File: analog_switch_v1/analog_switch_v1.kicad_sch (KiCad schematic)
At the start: 46 parts, among them J1 Conn_02x05_Odd_Even, J2 Audio In, J3 Audio Out, J4 Gate In, Q1 BC547, Q2 BC547, Q3 BC547, SW1 SW_GATE, U1 L78L05_SOT89, U2 TL072, U3 DG418LDJ

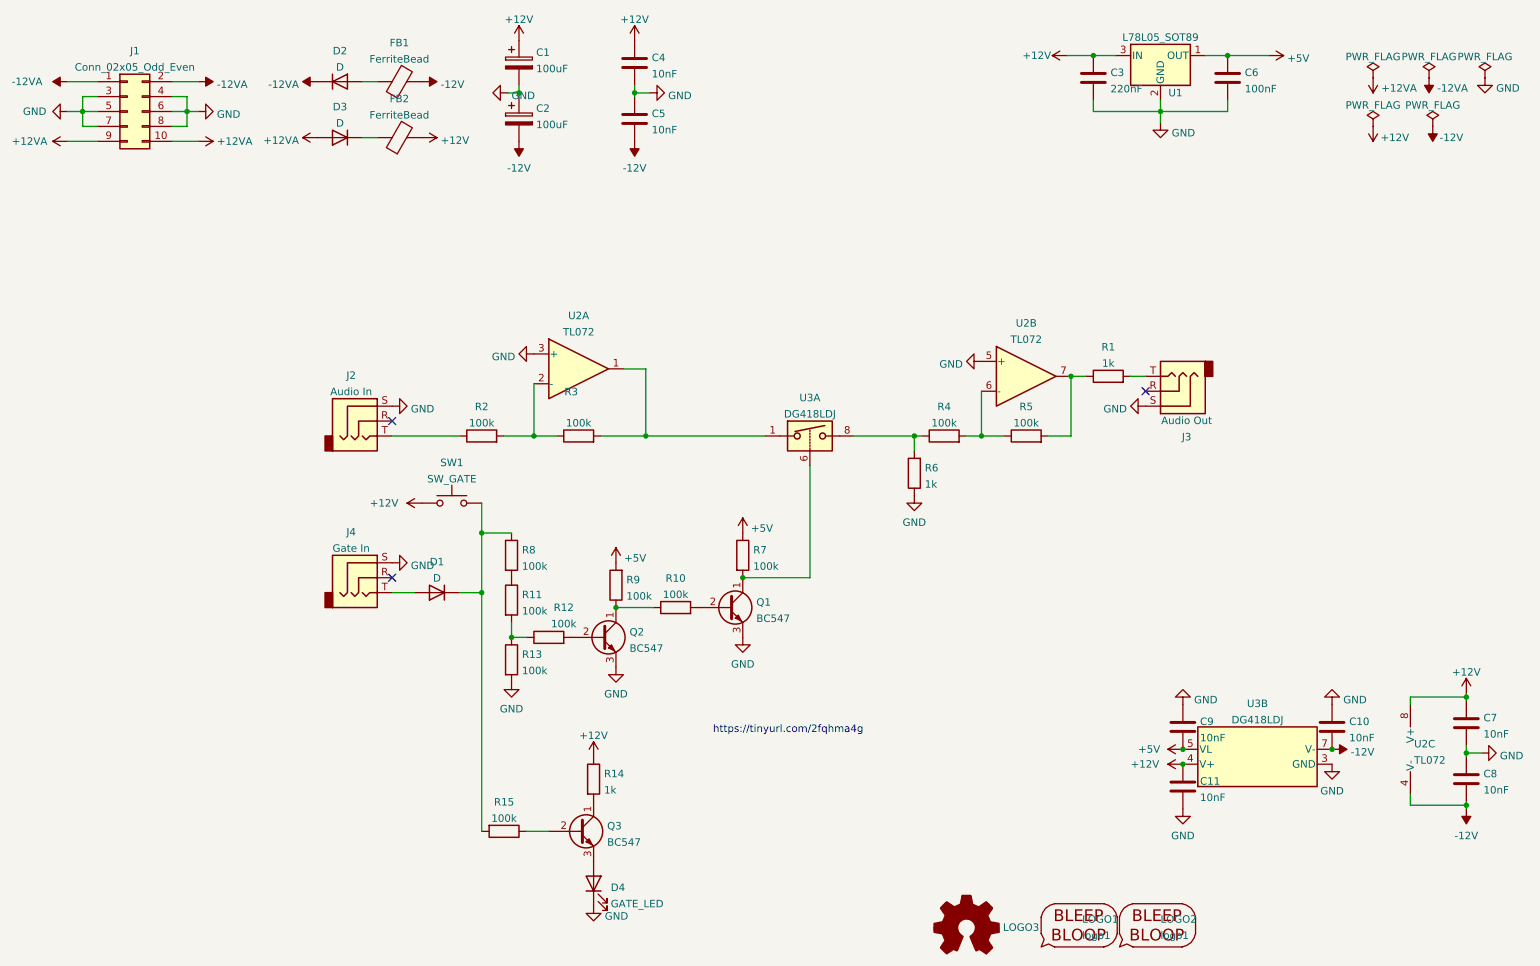
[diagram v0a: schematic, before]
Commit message: Geographic re-annotate and silkscreen cleanup
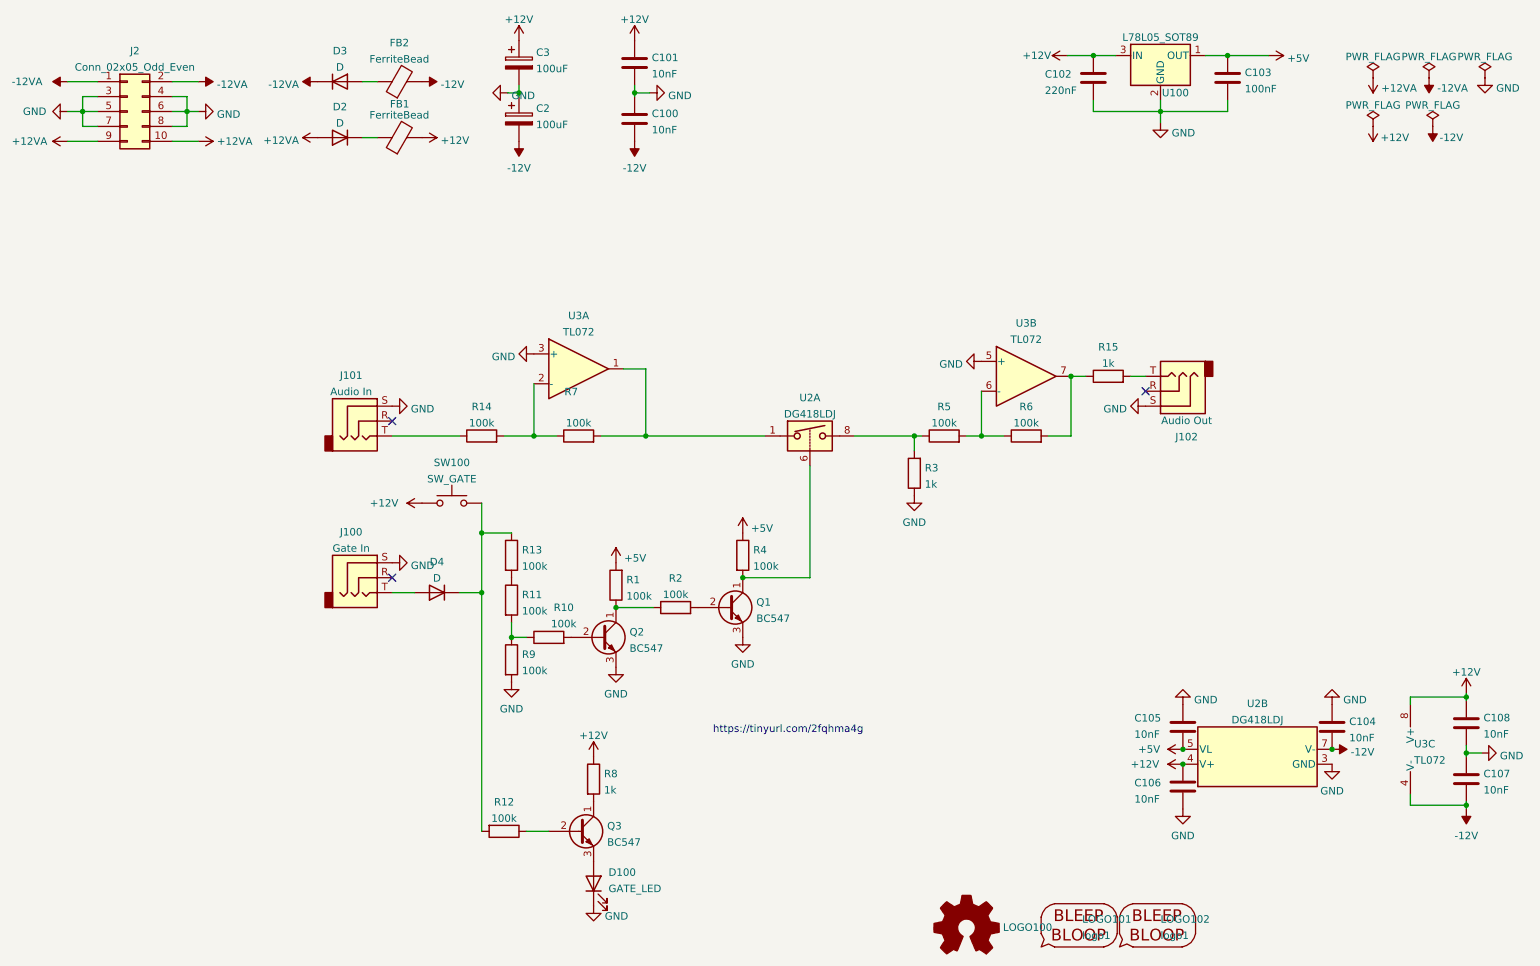
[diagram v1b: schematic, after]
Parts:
- renumbered C5 to C100, C4 to C101, C3 to C102, C6 to C103, C10 to C104, C9 to C105, C11 to C106, C8 to C107, C7 to C108, C1 to C3, D4 to D100, D3 to D2, D2 to D3, D1 to D4, FB2 to FB1, FB1 to FB2, J4 to J100, J2 to J101, J3 to J102, J1 to J2, LOGO3 to LOGO100, LOGO1 to LOGO101, LOGO2 to LOGO102, R9 to R1, R12 to R10, R15 to R12, R8 to R13, R2 to R14, R1 to R15, R10 to R2, R6 to R3, R7 to R4, R4 to R5, R5 to R6, R3 to R7, R14 to R8, R13 to R9, SW1 to SW100, U1 to U100, U3 to U2, U2 to U3
